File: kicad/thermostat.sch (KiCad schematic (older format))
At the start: 71 parts, among them IC1 LM2596S-5, J1 Conn_01x05, J2 Conn_02x02_Top_Bottom, J3 Conn_01x04, J4 Conn_01x04, J6 Screw_Terminal_01x05, T1 SIR434DN, T2 SIR434DN, U1 MCP23017_ML, U11 LTC4041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

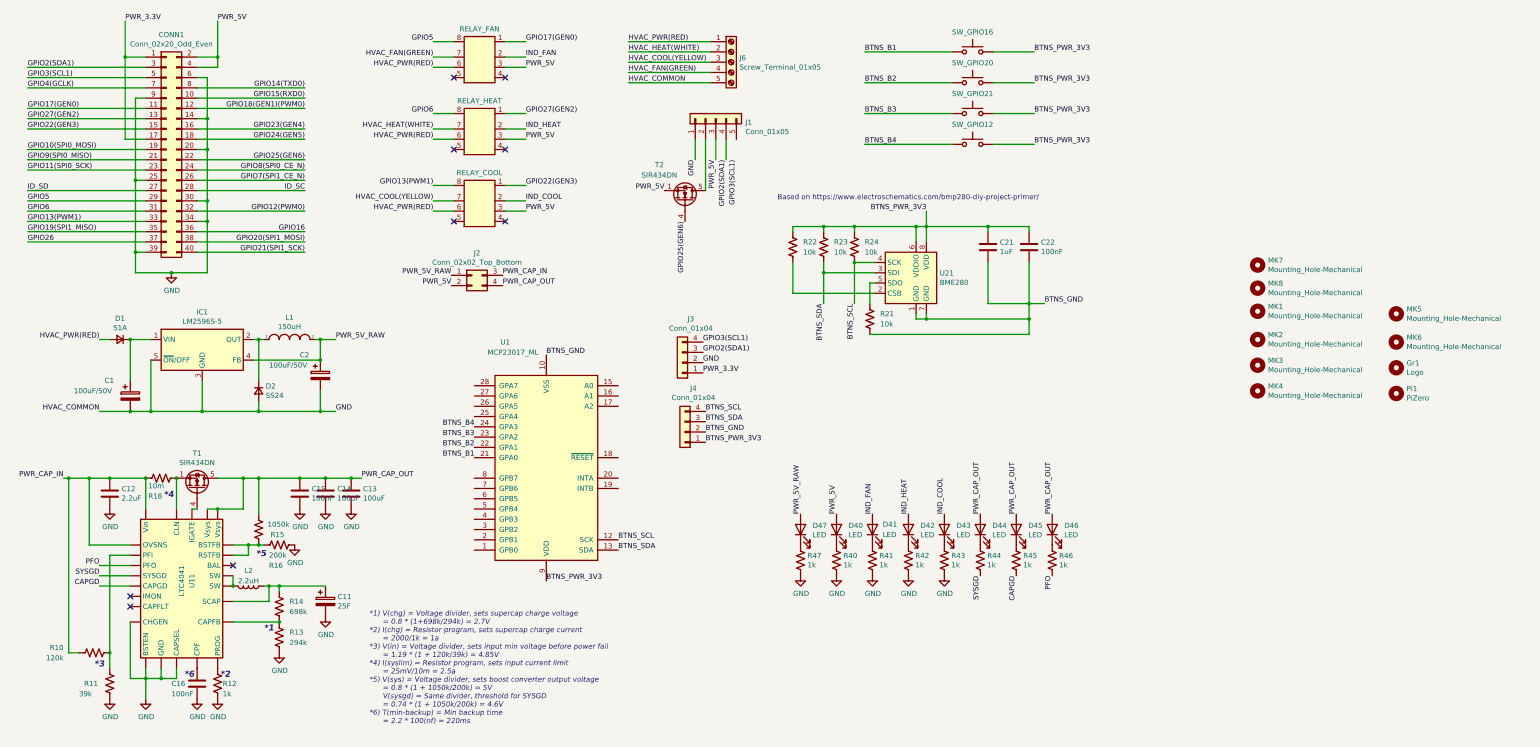
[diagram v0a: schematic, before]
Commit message: more updates, i2c changes for breakout almost ready
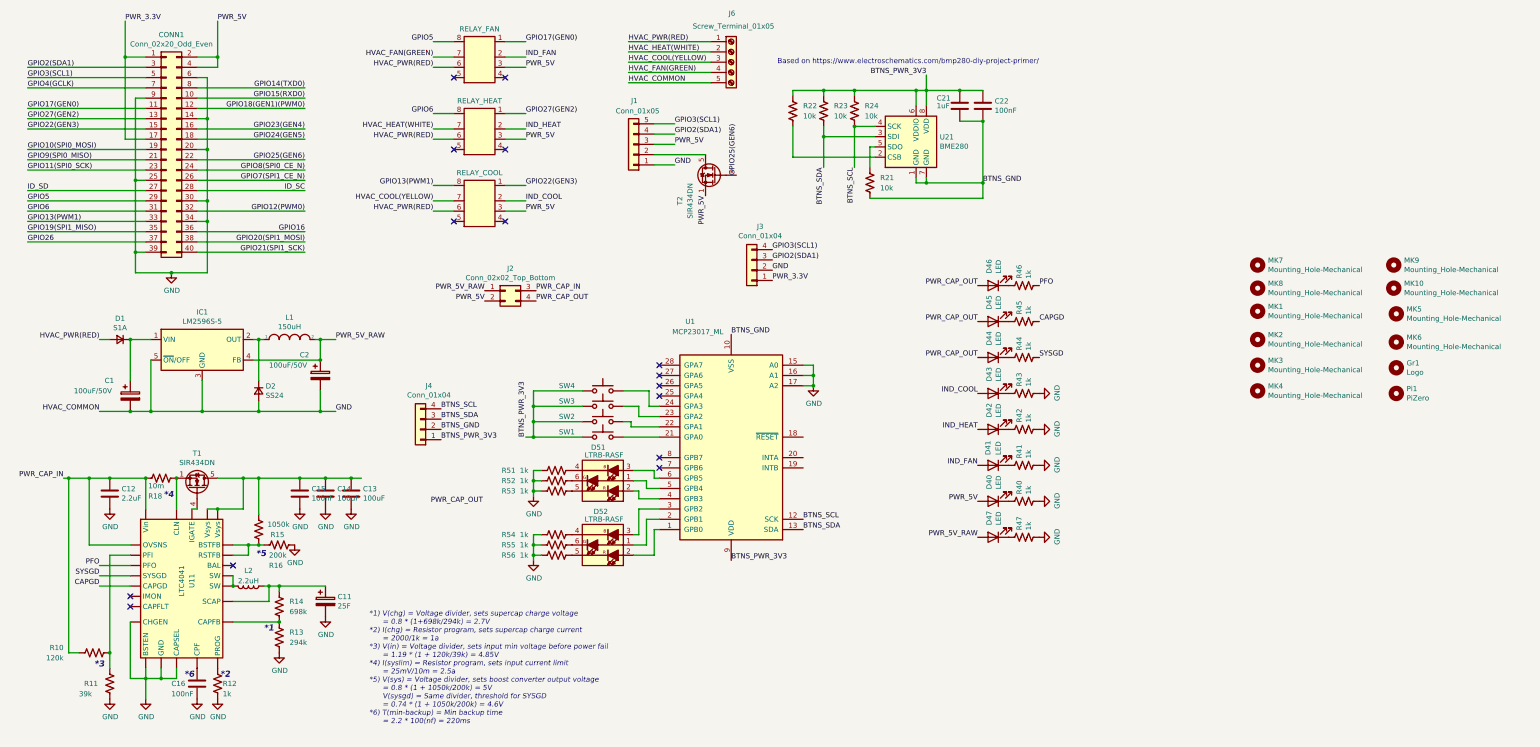
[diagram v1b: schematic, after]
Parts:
- added D51, D52: LTRB-RASF, Package_TO_SOT_SMD:SOT-23-6, symbol thermostat:LTRB-RASF
- added MK10, MK9: Mounting_Hole-Mechanical, MountingHole:MountingHole_2.5mm, symbol thermostat:Mounting_Hole-Mechanical
- added R51, R52, R53, R54, R55, R56: 1k, Resistor_SMD:R_0805_2012Metric, symbol Device:R_US
- SW1: renamed from SW_GPIO12; value GPIO12 -> Button
- SW2: renamed from SW_GPIO21; value GPIO21 -> Button
- SW3: renamed from SW_GPIO20; value GPIO20 -> Button
- SW4: renamed from SW_GPIO16; value GPIO16 -> Button
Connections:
- net BTNS_PWR_3V3: now also SW1.1, SW2.1, SW3.1, SW4.1; no longer SW1.2, SW2.2, SW3.2, SW4.2
- net GND: now also U1.15 (A0), U1.16 (A1), U1.17 (A2), R51.1, R52.1, R53.1, R54.1, R55.1, R56.1
- net GPIO3(SCL1): now also J1.5 (Pin_5)
- net PWR_CAP_OUT: no longer C13.1, C14.1, C15.1, R15.2, T1.5 (D), U11.1 (Vsys), U11.24 (Vsys)
- net at U1.1 (GPB0): now also D52.2 (AR)
- net at U1.2 (GPB1): now also D52.1 (AG)
- net at U1.3 (GPB2): now also D52.3 (AB)
- net at U1.4 (GPB3): now also D51.2 (AR)
- net at U1.5 (GPB4): now also D51.1 (AG)
- net at U1.6 (GPB5): now also D51.3 (AB)
- net BTNS_B1: no longer names the net of U1.21 (GPA0)
- net BTNS_B1: now also SW1.2; no longer SW4.1
- net BTNS_B2: no longer names the net of U1.22 (GPA1)
- net BTNS_B2: now also SW2.2; no longer SW3.1
- net BTNS_B3: no longer names the net of U1.23 (GPA2)
- net BTNS_B3: now also SW3.2; no longer SW2.1
- net BTNS_B4: no longer names the net of U1.24 (GPA3)
- net BTNS_B4: now also SW4.2; no longer SW1.1
- new net: C13.1, C14.1, C15.1, R15.2, T1.5 (D), U11.1 (Vsys), U11.24 (Vsys)
- new net: D51.4 (KB), R51.2
- new net: D51.5 (KR), R53.2
- new net: D51.6 (KG), R52.2
- new net: D52.4 (KB), R54.2
- new net: D52.5 (KR), R56.2
- new net: D52.6 (KG), R55.2
- no-connect marks 9 -> 15
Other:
- moved on the sheet: C21, C22, D40, D41, D42, D43, D44, D45, D46, D47, J1, J2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

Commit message: almost ready to route
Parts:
- removed MK6: Mounting_Hole-Mechanical, MountingHole:MountingHole_5mm_Pad, symbol thermostat:Mounting_Hole-Mechanical
- MK1, MK10, MK2, MK3, MK4, MK5, MK7, MK8, MK9: value Mounting_Hole-Mechanical -> Mounting Hole
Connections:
- net BTNS_GND: now also R51.1, R52.1, R53.1, R54.1, R55.1, R56.1, U1.15 (A0), U1.16 (A1), U1.17 (A2)
- net BTNS_PWR_3V3: now also U1.18 (~RESET~); no longer SW1.1, SW2.1, SW3.1, SW4.1
- net GND: no longer R51.1, R52.1, R53.1, R54.1, R55.1, R56.1, U1.15 (A0), U1.16 (A1), U1.17 (A2)
- net PWR_CAP_OUT: now also C13.1, C14.1, C15.1, R15.2, T1.5 (D), U11.1 (Vsys), U11.24 (Vsys)
- new net: SW1.1, SW2.1, SW3.1, SW4.1
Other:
- note added: "## addr=0x20 ##"
- note added: "## addr=0x27 ##"
- note added: "## addr=0x76 ##"
- moved on the sheet: C21, C22, D40, D41, D42, D43, D44, D45, D46, D47, D51, D52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

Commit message: half routed
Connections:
- net BTNS_PWR_3V3: now also SW1.1, SW2.1, SW3.1, SW4.1
- net at SW4.2: now also U1.22 (GPA1); no longer U1.24 (GPA3)
- net at SW3.2: now also U1.21 (GPA0); no longer U1.23 (GPA2)
- net at SW2.2: now also U1.4 (GPB3); no longer U1.22 (GPA1)
- net at SW1.2: now also U1.5 (GPB4); no longer U1.21 (GPA0)
- net at U1.1 (GPB0): now also D52.3 (AB); no longer D52.2 (AR)
- net at U1.2 (GPB1): now also D52.2 (AR); no longer D52.1 (AG)
- net at U1.26 (GPA5): now also D51.3 (AB)
- net at U1.27 (GPA6): now also D51.2 (AR)
- net at U1.28 (GPA7): now also D51.1 (AG)
- net at U1.3 (GPB2): now also D52.1 (AG); no longer D52.3 (AB)
- net at U1.6 (GPB5): no longer D51.3 (AB)
- no-connect marks 15 -> 31
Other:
- moved on the sheet: D51, D52, R51, R52, R53, R54, R55, R56, SW1, SW2, SW3, SW4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

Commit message: design v2.2 sent to fab
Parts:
- C12: MPN (none) -> 581-08053C225K4T2A
- C13, C14: MPN (none) -> 81-GRM21BR60J107ME5L
- C15, C16, C22: MPN (none) -> 80-C0805X104K5R3316
- C21: MPN (none) -> 80-C0805C105M8RAUTO
- D40, D41, D44, D45, D46, D47: value LED -> Green; MPN (none) -> 710-150080GS75000
- D42: value LED -> Red; MPN (none) -> 710-150080RS75000
- D43: value LED -> Blue; MPN (none) -> 710-150080BS75000
- D51, D52: value LTRB-RASF -> RGB; MPN (none) -> 720-LTRBRASFA6660; Mouser (none) -> 720-LTRBRASFA6660
- IC1: MPN 926-LM2596S-50 -> 926-LM2596S-5.0/NOPB; Mouser 926-LM2596S-50 -> 926-LM2596S-5.0/NOPB
- RELAY1: value RELAY_FAN -> RELAY
- RELAY2: value RELAY_HEAT -> RELAY
- RELAY3: value RELAY_COOL -> RELAY
- U1: MPN (none) -> 579-MCP23017T-E/ML
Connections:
- net GPIO12(PWM0): now also RELAY1.8
- net GPIO13(PWM1): no longer RELAY3.8
- net GPIO16: now also RELAY3.8
- net GPIO17(GEN0): no longer RELAY1.1
- net GPIO19(SPI1_MISO): now also RELAY3.1
- net GPIO20(SPI1_MOSI): now also RELAY2.1
- net GPIO21(SPI1_SCK): now also RELAY2.8
- net GPIO22(GEN3): no longer RELAY3.1
- net GPIO25(GEN6): no longer T2.4 (G)
- net GPIO26: now also T2.4 (G)
- net GPIO27(GEN2): no longer RELAY2.1
- net GPIO5: no longer RELAY1.8
- net GPIO6: now also RELAY1.1; no longer RELAY2.8
- no-connect marks 31 -> 36
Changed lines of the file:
@@
 P 7100 1275
 F 0 "RELAY1" V 7250 1475 50  0001 C CNN
-F 1 "RELAY_FAN" H 7100 1598 50  0000 C CNN
+F 1 "RELAY" H 7100 1598 50  0000 C CNN
 F 2 "project_footprints:AGQ210A03" V 7250 1475 50  0001 C CNN
 F 3 "https://www.mouser.com/datasheet/2/315/mech_eng_gq-1299323.pdf" V 7250 1475 50  0001 C CNN
@@
 $EndComp
 Text Label 7350 1075 0    50   ~ 0
-GPIO17(GEN0)
+GPIO6
 Text Label 6850 1325 2    50   ~ 0
 HVAC_PWR(RED)
@@
 P 7100 1975
 F 0 "RELAY2" V 7250 2175 50  0001 C CNN
-F 1 "RELAY_HEAT" H 7100 2298 50  0000 C CNN
+F 1 "RELAY" H 7100 2298 50  0000 C CNN
 F 2 "project_footprints:AGQ210A03" V 7250 2175 50  0001 C CNN
 F 3 "https://www.mouser.com/datasheet/2/315/mech_eng_gq-1299323.pdf" V 7250 2175 50  0001 C CNN
@@
 $EndComp
 Text Label 7350 1775 0    50   ~ 0
-GPIO27(GEN2)
+GPIO20(SPI1_MOSI)
 Text Label 6850 1775 2    50   ~ 0
-GPIO6
+GPIO21(SPI1_SCK)
 Text Label 6850 1925 2    50   ~ 0
 HVAC_HEAT(WHITE)
@@
 P 7100 2675
 F 0 "RELAY3" V 7250 2875 50  0001 C CNN
-F 1 "RELAY_COOL" H 7100 2998 50  0000 C CNN
+F 1 "RELAY" H 7100 2998 50  0000 C CNN
 F 2 "project_footprints:AGQ210A03" V 7250 2875 50  0001 C CNN
 F 3 "https://www.mouser.com/datasheet/2/315/mech_eng_gq-1299323.pdf" V 7250 2875 50  0001 C CNN
@@
 $EndComp
 Text Label 7350 2475 0    50   ~ 0
-GPIO22(GEN3)
+GPIO19(SPI1_MISO)
 Text Label 6850 2475 2    50   ~ 0
-GPIO13(PWM1)
+GPIO16
 Text Label 6850 2625 2    50   ~ 0
 HVAC_COOL(YELLOW)
@@
 F 2 "Package_TO_SOT_SMD:TO-263-5_TabPin3" H 2500 3700 50  0001 L CIN
 F 3 "http://www.ti.com/lit/ds/symlink/lm2596.pdf" H 2450 3950 50  0001 C CNN
-F 4 "926-LM2596S-50" H 2450 3950 50  0001 C CNN "Mouser"
+F 4 "926-LM2596S-5.0/NOPB" H 2450 3950 50  0001 C CNN "Mouser"
 F 5 "1" H 2450 3950 50  0001 C CNN "Populate"
-F 6 "926-LM2596S-50" H 2450 3950 50  0001 C CNN "MPN"
+F 6 "926-LM2596S-5.0/NOPB" H 2450 3950 50  0001 C CNN "MPN"
 	1    2450 3950
 	1    0    0    -1
@@
 HVAC_FAN(GREEN)
 Text Label 6850 1075 2    50   ~ 0
-GPIO5
+GPIO12(PWM0)
 Text Notes 8200 725  0    50   ~ 0
 Based on https://www.electroschematics.com/bmp280-diy-project-primer/
@@
 P 10300 3625
 F 0 "D40" V 10339 3508 50  0000 R CNN
-F 1 "LED" V 10248 3508 50  0000 R CNN
+F 1 "Green" V 10248 3508 50  0000 R CNN
 F 2 "LED_SMD:LED_0805_2012Metric" H 10300 3625 50  0001 C CNN
 F 3 "~" H 10300 3625 50  0001 C CNN
 F 4 "1" H 10300 3625 50  0001 C CNN "Populate"
 F 5 "710-150080GS75000" H 10300 3625 50  0001 C CNN "Mouser"
+F 6 "710-150080GS75000" H 10300 3625 50  0001 C CNN "MPN"
 	1    10300 3625
 	-1   0    0    1
@@
 P 8850 2525
 F 0 "D43" V 8889 2408 50  0000 R CNN
-F 1 "LED" V 8798 2408 50  0000 R CNN
+F 1 "Blue" V 8798 2408 50  0000 R CNN
 F 2 "LED_SMD:LED_0805_2012Metric" H 8850 2525 50  0001 C CNN
 F 3 "~" H 8850 2525 50  0001 C CNN
 F 4 "1" H 8850 2525 50  0001 C CNN "Populate"
 F 5 "710-150080BS75000" H 8850 2525 50  0001 C CNN "Mouser"
+F 6 "710-150080BS75000" H 8850 2525 50  0001 C CNN "MPN"
 	1    8850 2525
 	-1   0    0    1
@@
 P 8850 3225
 F 0 "D41" V 8900 3125 50  0000 R CNN
-F 1 "LED" V 8800 3125 50  0000 R CNN
+F 1 "Green" V 8800 3125 50  0000 R CNN
 F 2 "LED_SMD:LED_0805_2012Metric" H 8850 3225 50  0001 C CNN
 F 3 "~" H 8850 3225 50  0001 C CNN
 F 4 "1" H 8850 3225 50  0001 C CNN "Populate"
 F 5 "710-150080GS75000" H 8850 3225 50  0001 C CNN "Mouser"
+F 6 "710-150080GS75000" H 8850 3225 50  0001 C CNN "MPN"
 	1    8850 3225
 	-1   0    0    1
@@
 P 8850 2875
 F 0 "D42" V 8889 2758 50  0000 R CNN
-F 1 "LED" V 8798 2758 50  0000 R CNN
+F 1 "Red" V 8798 2758 50  0000 R CNN
 F 2 "LED_SMD:LED_0805_2012Metric" H 8850 2875 50  0001 C CNN
 F 3 "~" H 8850 2875 50  0001 C CNN
 F 4 "1" H 8850 2875 50  0001 C CNN "Populate"
 F 5 "710-150080RS75000" H 8850 2875 50  0001 C CNN "Mouser"
+F 6 "710-150080RS75000" H 8850 2875 50  0001 C CNN "MPN"
 	1    8850 2875
 	-1   0    0    1
@@
 P 10300 3275
 F 0 "D44" V 10339 3158 50  0000 R CNN
-F 1 "LED" V 10248 3158 50  0000 R CNN
+F 1 "Green" V 10248 3158 50  0000 R CNN
 F 2 "LED_SMD:LED_0805_2012Metric" H 10300 3275 50  0001 C CNN
 F 3 "~" H 10300 3275 50  0001 C CNN
 F 4 "1" H 10300 3275 50  0001 C CNN "Populate"
 F 5 "710-150080GS75000" H 10300 3275 50  0001 C CNN "Mouser"
+F 6 "710-150080GS75000" H 10300 3275 50  0001 C CNN "MPN"
 	1    10300 3275
 	-1   0    0    1
@@
 P 10300 2925
 F 0 "D45" V 10339 2808 50  0000 R CNN
-F 1 "LED" V 10248 2808 50  0000 R CNN
+F 1 "Green" V 10248 2808 50  0000 R CNN
 F 2 "LED_SMD:LED_0805_2012Metric" H 10300 2925 50  0001 C CNN
 F 3 "~" H 10300 2925 50  0001 C CNN
 F 4 "1" H 10300 2925 50  0001 C CNN "Populate"
 F 5 "710-150080GS75000" H 10300 2925 50  0001 C CNN "Mouser"
+F 6 "710-150080GS75000" H 10300 2925 50  0001 C CNN "MPN"
 	1    10300 2925
 	-1   0    0    1
@@
 P 10300 2575
 F 0 "D46" V 10339 2458 50  0000 R CNN
-F 1 "LED" V 10248 2458 50  0000 R CNN
+F 1 "Green" V 10248 2458 50  0000 R CNN
 F 2 "LED_SMD:LED_0805_2012Metric" H 10300 2575 50  0001 C CNN
 F 3 "~" H 10300 2575 50  0001 C CNN
 F 4 "1" H 10300 2575 50  0001 C CNN "Populate"
 F 5 "710-150080GS75000" H 10300 2575 50  0001 C CNN "Mouser"
+F 6 "710-150080GS75000" H 10300 2575 50  0001 C CNN "MPN"
 	1    10300 2575
 	-1   0    0    1
@@
 P 8850 3575
 F 0 "D47" V 8889 3458 50  0000 R CNN
-F 1 "LED" V 8798 3458 50  0000 R CNN
+F 1 "Green" V 8798 3458 50  0000 R CNN
 F 2 "LED_SMD:LED_0805_2012Metric" H 8850 3575 50  0001 C CNN
 F 3 "~" H 8850 3575 50  0001 C CNN
 F 4 "1" H 8850 3575 50  0001 C CNN "Populate"
 F 5 "710-150080GS75000" H 8850 3575 50  0001 C CNN "Mouser"
+F 6 "710-150080GS75000" H 8850 3575 50  0001 C CNN "MPN"
 	1    8850 3575
 	-1   0    0    1
@@
 F 4 "80-C0805X104K5R3316" H 2400 7200 50  0001 C CNN "Mouser"
 F 5 "1" H 2400 7200 50  0001 C CNN "Populate"
+F 6 "80-C0805X104K5R3316" H 2400 7200 50  0001 C CNN "MPN"
 	1    2400 7200
 	1    0    0    -1
@@
 F 4 "581-08053C225K4T2A" H 1550 5350 50  0001 C CNN "Mouser"
 F 5 "1" H 1550 5350 50  0001 C CNN "Populate"
+F 6 "581-08053C225K4T2A" H 1550 5350 50  0001 C CNN "MPN"
 	1    1550 5350
 	1    0    0    -1
@@
 F 4 "80-C0805X104K5R3316" H 3400 5350 50  0001 C CNN "Mouser"
 F 5 "1" H 3400 5350 50  0001 C CNN "Populate"
+F 6 "80-C0805X104K5R3316" H 3400 5350 50  0001 C CNN "MPN"
 	1    3400 5350
 	1    0    0    -1
@@
 F 4 "81-GRM21BR60J107ME5L" H 3650 5350 50  0001 C CNN "Mouser"
 F 5 "1" H 3650 5350 50  0001 C CNN "Populate"
+F 6 "81-GRM21BR60J107ME5L" H 3650 5350 50  0001 C CNN "MPN"
 	1    3650 5350
 	1    0    0    -1
@@
 F 4 "81-GRM21BR60J107ME5L" H 3900 5350 50  0001 C CNN "Mouser"
 F 5 "1" H 3900 5350 50  0001 C CNN "Populate"
+F 6 "81-GRM21BR60J107ME5L" H 3900 5350 50  0001 C CNN "MPN"
 	1    3900 5350
 	1    0    0    -1
@@
 $EndComp
 Text Label 5375 2500 1    50   ~ 0
-GPIO25(GEN6)
+GPIO26
 Text Label 5075 2700 0    50   ~ 0
 PWR_5V
@@
 P 5850 5775
 F 0 "D52" H 5675 5450 50  0000 L CNN
-F 1 "LTRB-RASF" H 5650 5525 50  0000 L CNN
+F 1 "RGB" H 5650 5525 50  0000 L CNN
 F 2 "Package_TO_SOT_SMD:SOT-23-6" H 5650 5455 50  0001 L CNN
 F 3 "https://dammedia.osram.info/media/resource/hires/osram-dam-3950803/LTRB%20RASF_EN.pdf" H 6000 5775 50  0001 L CNN
+F 4 "720-LTRBRASFA6660" H 5850 5775 50  0001 C CNN "MPN"
+F 5 "720-LTRBRASFA6660" H 5850 5775 50  0001 C CNN "Mouser"
 	1    5850 5775
 	-1   0    0    1
@@
 P 5850 4050
 F 0 "D51" H 5650 3725 50  0000 L CNN
-F 1 "LTRB-RASF" H 5650 3800 50  0000 L CNN
+F 1 "RGB" H 5650 3800 50  0000 L CNN
 F 2 "Package_TO_SOT_SMD:SOT-23-6" H 5650 3730 50  0001 L CNN
 F 3 "https://dammedia.osram.info/media/resource/hires/osram-dam-3950803/LTRB%20RASF_EN.pdf" H 6000 4050 50  0001 L CNN
+F 4 "720-LTRBRASFA6660" H 5850 4050 50  0001 C CNN "MPN"
+F 5 "720-LTRBRASFA6660" H 5850 4050 50  0001 C CNN "Mouser"
 	1    5850 4050
 	-1   0    0    1
@@
 F 4 "80-C0805X104K5R3316" H 10200 1125 50  0001 C CNN "Mouser"
 F 5 "1" H 10200 1125 50  0001 C CNN "Populate"
+F 6 "80-C0805X104K5R3316" H 10200 1125 50  0001 C CNN "MPN"
 	1    10200 1125
 	1    0    0    -1
@@
 F 4 "80-C0805C105M8RAUTO" H 9975 1125 50  0001 C CNN "Mouser"
 F 5 "1" H 9975 1125 50  0001 C CNN "Populate"
+F 6 "80-C0805C105M8RAUTO" H 9975 1125 50  0001 C CNN "MPN"
 	1    9975 1125
 	1    0    0    -1
@@
 F 3 "http://ww1.microchip.com/downloads/en/DeviceDoc/20001952C.pdf" H 7300 3725 50  0001 L CNN
 F 4 "579-MCP23017T-E/ML" H 7100 4825 50  0001 C CNN "Mouser"
+F 5 "579-MCP23017T-E/ML" H 7100 4825 50  0001 C CNN "MPN"
 	1    7100 4825
 	-1   0    0    1
@@
 NoConn ~ 2400 2400
 NoConn ~ 1900 2400
-NoConn ~ 2400 2600
-NoConn ~ 2400 2800
-NoConn ~ 2400 2900
-NoConn ~ 2400 3000
-NoConn ~ 1900 2900
-NoConn ~ 1900 2800
 Wire Wire Line
 	6400 5625 6150 5625
@@
 Wire Wire Line
 	6050 5225 6050 5325
+NoConn ~ 1900 2500
+NoConn ~ 1900 2700
+NoConn ~ 1900 1600
+NoConn ~ 1900 1700
+NoConn ~ 1900 1800
+NoConn ~ 2400 2100
+NoConn ~ 6400 4425
+NoConn ~ 6400 4925
+NoConn ~ 6400 5025
+NoConn ~ 6400 5125
+NoConn ~ 6400 4525
 $EndSCHEMATC

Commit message: updates, cad broken
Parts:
- U1: symbol Interface_Expansion:MCP23017_SO -> Interface_Expansion:MCP23017_ML
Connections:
- wire segments 206 -> 208
- no-connect marks 36 -> 30
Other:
- moved on the sheet: D51, D52, R51, R52, R53, R54, R55, R56, SW1, SW2, SW3, SW4

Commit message: Re-route 23017
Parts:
- U1: MPN 579-MCP23017T-E/ML -> (none); Mouser 579-MCP23017T-E/ML -> (none)
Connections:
- net labels added: BTNS_INT
- wire segments 208 -> 219
- no-connect marks 30 -> 35
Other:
- moved on the sheet: D51, D52, R51, R52, R53, R54, R55, R56, SW1, SW2, SW3, SW4
